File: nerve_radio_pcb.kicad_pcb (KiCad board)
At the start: 4 copper layers, 50 x 50 mm, 12 parts, among them J1 2x15, J2 5V UART Breakout, J3 3V SPI Breakout, J4 5V GPIO Breakout, U1 XBP9B-DMWT-002, U2 TXB0104QPWRQ1

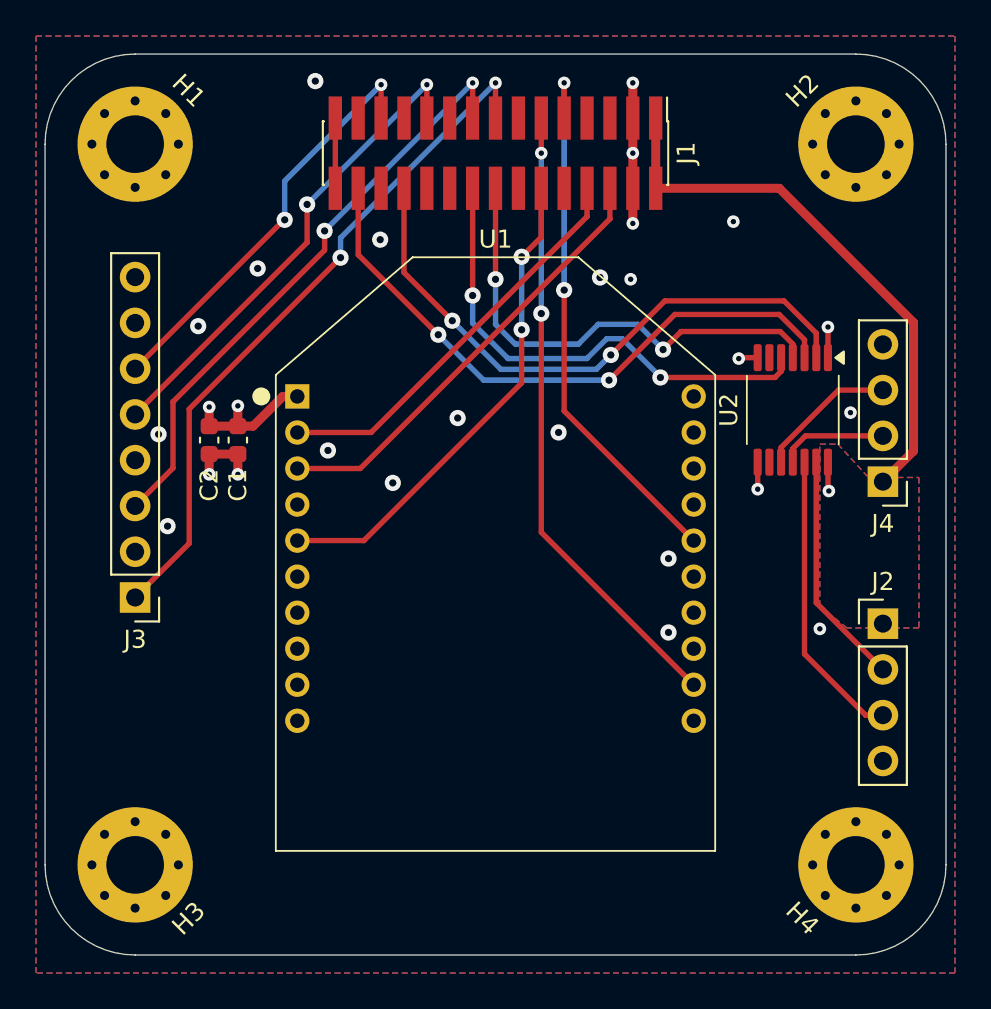
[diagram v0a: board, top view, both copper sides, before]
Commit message: Add ground stitching vias and silkscreen cleanup
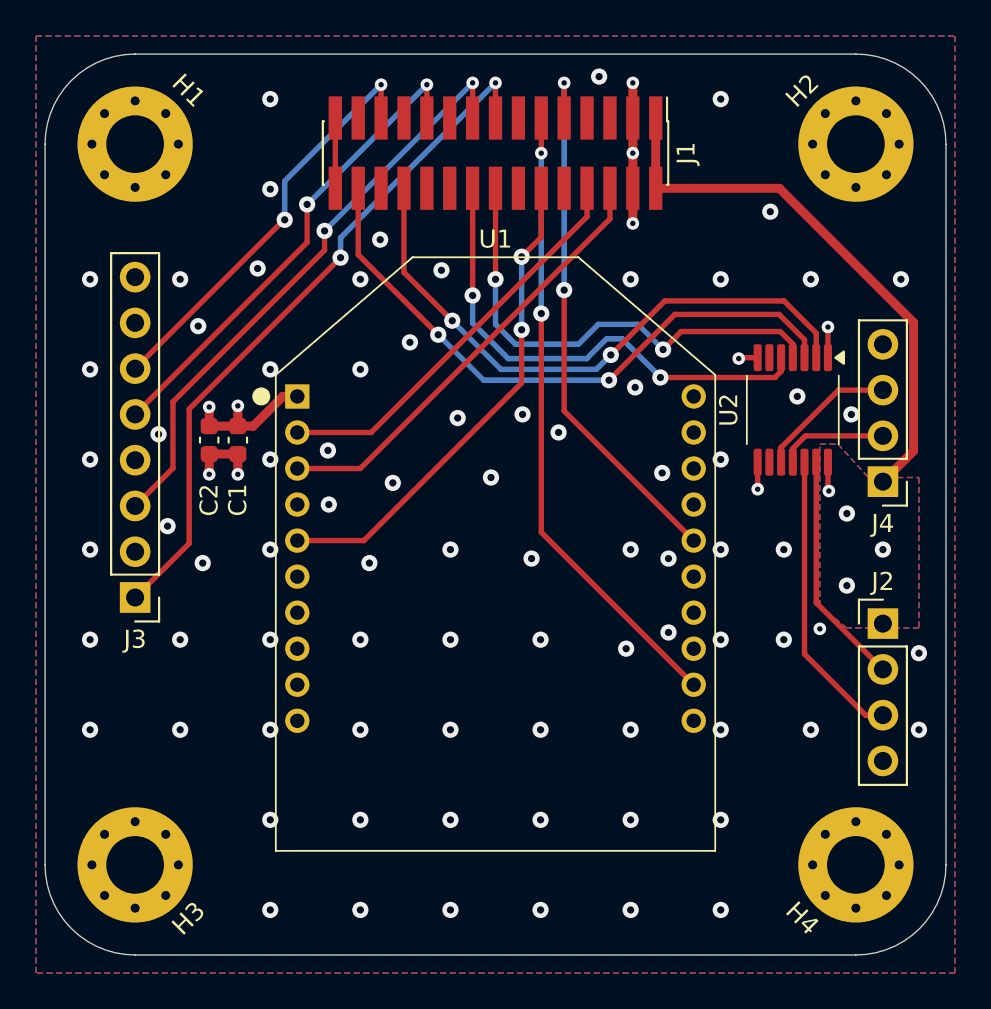
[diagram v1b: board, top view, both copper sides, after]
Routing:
- net GND: vias 20 -> 83
- net +5V: vias 1 -> 4

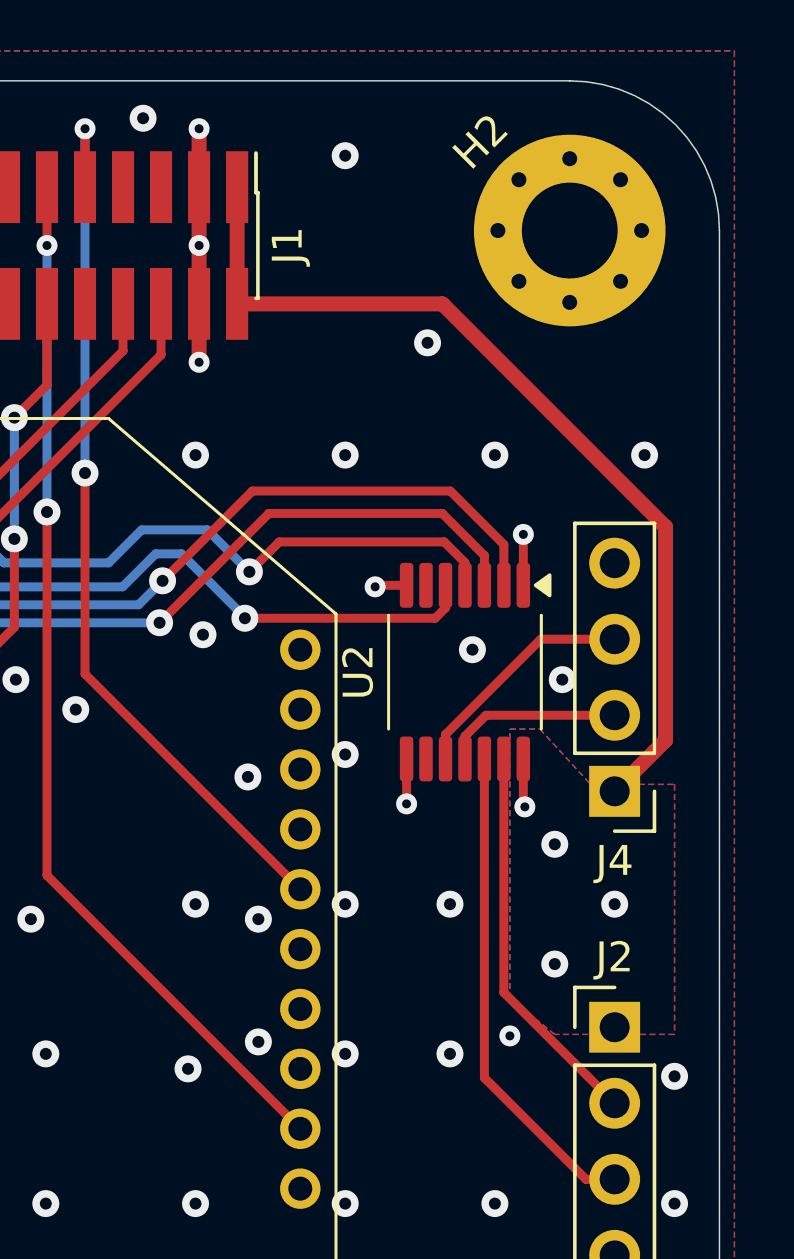
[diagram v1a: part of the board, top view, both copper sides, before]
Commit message: Widen 5V rail
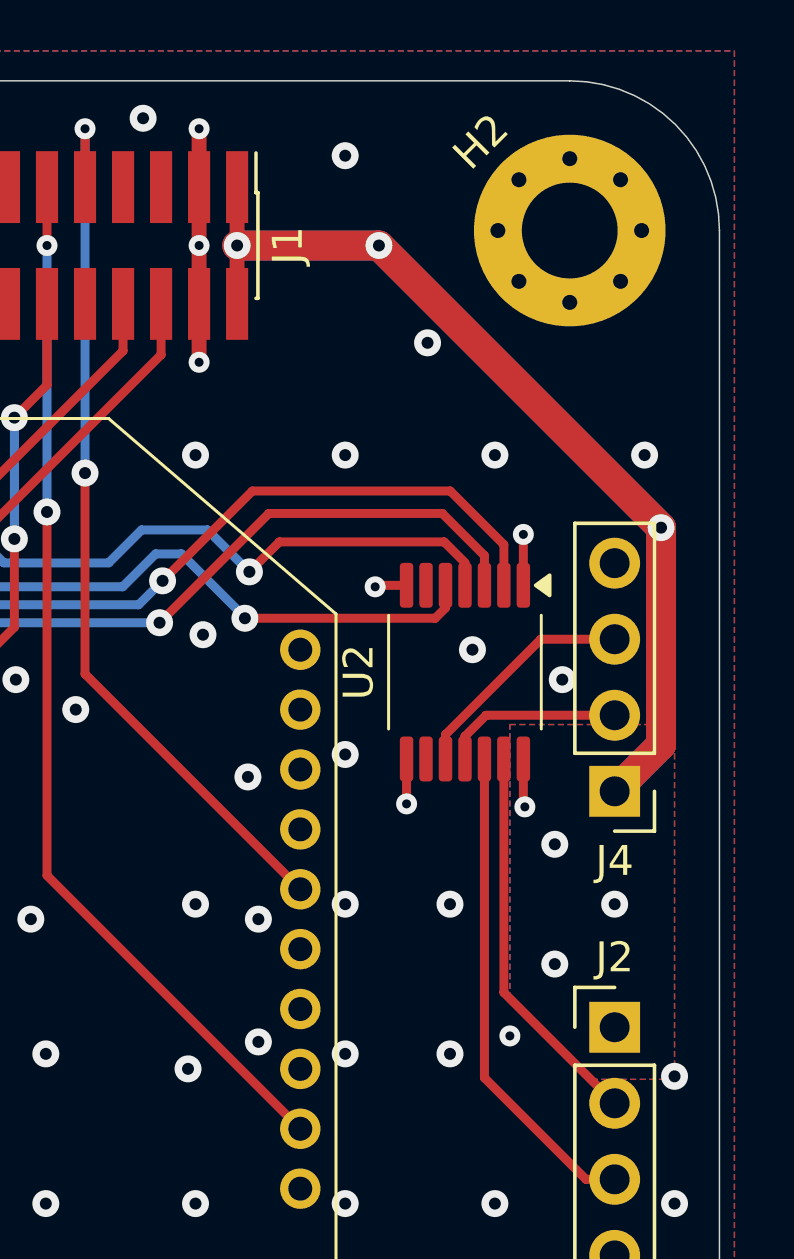
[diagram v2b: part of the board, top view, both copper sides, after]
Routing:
- net +5V: track 32.5 -> 60.5 mm, vias 4 -> 7
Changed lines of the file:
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@@
 	)
 	(segment
-		(start 157.39 83.55)
+		(start 171.55 102.18)
+		(end 171.55 94.923654)
+		(width 1)
+		(layer "F.Cu")
+		(net 4)
+	)
+	(segment
+		(start 157.39 85.5)
 		(end 157.39 87.45)
 		(width 0.5)
+		(layer "F.Cu")
+		(net 4)
+	)
+	(segment
+		(start 162.126346 85.5)
+		(end 157.39 85.5)
+		(width 1)
 		(layer "F.Cu")
 		(net 4)
@@
 	)
 	(segment
-		(start 171.7 94.9)
-		(end 171.7 102.03)
-		(width 0.5)
-		(layer "F.Cu")
-		(net 4)
-	)
-	(segment
 		(start 167 104.25)
 		(end 166.95 104.2)
@@
 	)
 	(segment
-		(start 164.25 87.45)
-		(end 171.7 94.9)
-		(width 0.5)
-		(layer "F.Cu")
-		(net 4)
-	)
-	(segment
-		(start 157.39 87.45)
-		(end 164.25 87.45)
-		(width 0.5)
-		(layer "F.Cu")
-		(net 4)
-	)
-	(segment
-		(start 171.7 102.03)
-		(end 170 103.73)
-		(width 0.5)
-		(layer "F.Cu")
+		(start 170 103.73)
+		(end 171.55 102.18)
+		(width 1)
+		(layer "F.Cu")
+		(net 4)
+	)
+	(segment
+		(start 171.55 94.923654)
+		(end 162.126346 85.5)
+		(width 1)
+		(layer "F.Cu")
+		(net 4)
+	)
+	(segment
+		(start 157.39 83.55)
+		(end 157.39 85.5)
+		(width 0.5)
+		(layer "F.Cu")
+		(net 4)
+	)
+	(via
+		(at 162.126346 85.5)
+		(size 0.9)
+		(drill 0.4)
+		(layers "F.Cu" "B.Cu")
 		(net 4)
 	)
@@
 	)
 	(via
+		(at 157.39 85.5)
+		(size 0.9)
+		(drill 0.4)
+		(layers "F.Cu" "B.Cu")
+		(net 4)
+	)
+	(via
 		(at 167 104.25)
 		(size 0.7)
@@
 		(layers "F.Cu" "B.Cu")
 		(free yes)
+		(net 4)
+	)
+	(via
+		(at 171.55 94.923654)
+		(size 0.9)
+		(drill 0.4)
+		(layers "F.Cu" "B.Cu")
+		(net 4)
+	)
+	(segment
+		(start 171.55 94.923654)
+		(end 162.126346 85.5)
+		(width 1)
+		(layer "B.Cu")
+		(net 4)
+	)
+	(segment
+		(start 171.55 102.18)
+		(end 171.55 94.923654)
+		(width 1)
+		(layer "B.Cu")
+		(net 4)
+	)
+	(segment
+		(start 170 103.73)
+		(end 171.55 102.18)
+		(width 1)
+		(layer "B.Cu")
+		(net 4)
+	)
+	(segment
+		(start 162.126346 85.5)
+		(end 157.39 85.5)
+		(width 1)
+		(layer "B.Cu")
 		(net 4)
 	)
@@
 		(polygon
 			(pts
-				(xy 172 111.85) (xy 168 111.85) (xy 166.5 110.65) (xy 166.5 101.65) (xy 167.5 101.65) (xy 169.2 103.5)
-				(xy 172 103.5)
+				(xy 172 113.35) (xy 169.25 113.35) (xy 166.5 110.65) (xy 166.5 101.5) (xy 172 101.5)
 			)
 		)

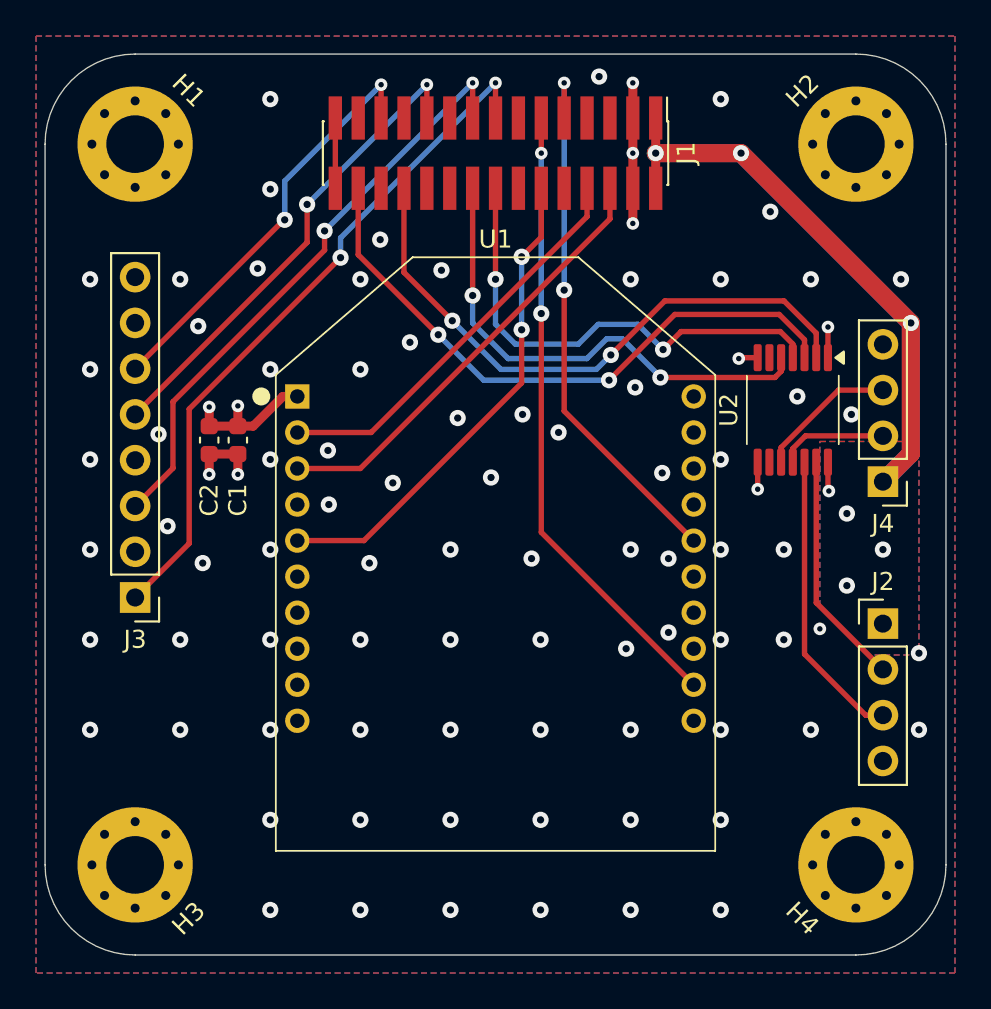
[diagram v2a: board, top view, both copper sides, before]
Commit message: Cleanup revision and docs pictures
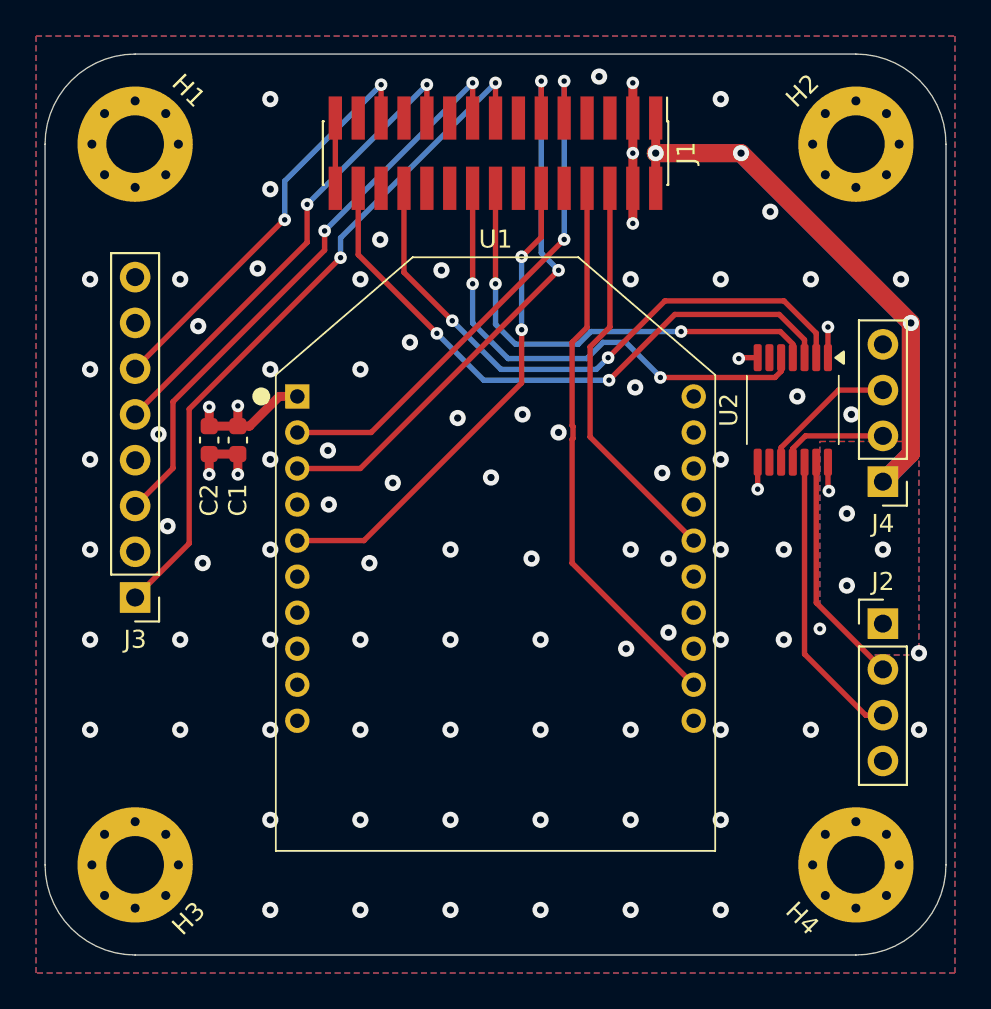
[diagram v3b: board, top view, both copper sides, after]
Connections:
- J1 pad 11: /RADIO_UART_CTS -> /RADIO_UART_TX
- J1 pad 6: /RADIO_UART_TX -> /RADIO_UART_RTS
- J1 pad 8: /RADIO_UART_RX -> /RADIO_UART_CTS
- J1 pad 9: /RADIO_UART_RTS -> /RADIO_UART_RX
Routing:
- net /RADIO_UART_RTS: track 30.3 -> 22.4 mm, vias 2 -> 0
- net /RADIO_UART_RX: track 22.6 -> 30.1 mm, vias 0 -> 2
- net /RADIO_UART_TX: track 24.8 -> 32.0 mm, vias 0 -> 2
- net /RADIO_UART_CTS: track 35.0 -> 30.7 mm, vias 2 -> 0
- net /GPIO_1: track 27.0 -> 25.8 mm

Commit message: Cleanup and update board-to-board connector
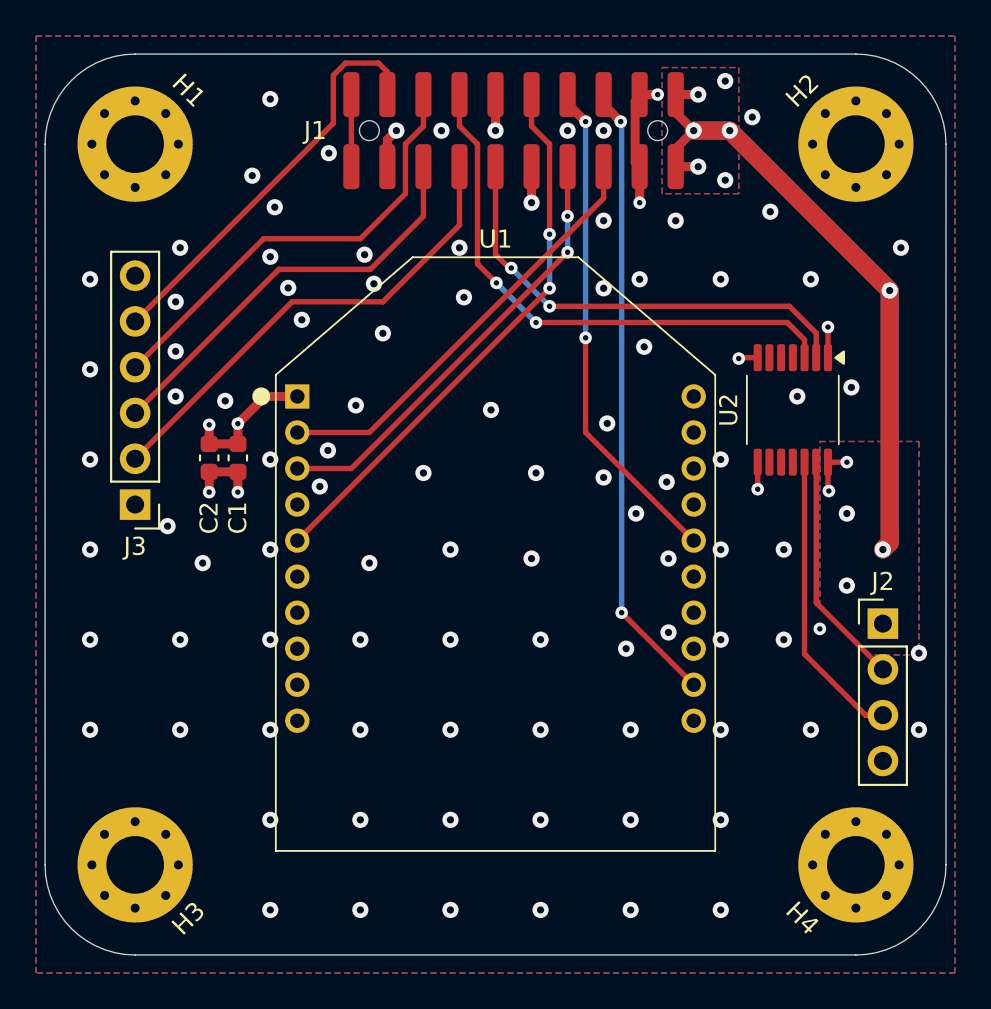
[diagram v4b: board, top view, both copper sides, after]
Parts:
- removed J4: 5V GPIO Breakout, Connector_PinHeader_2.54mm:PinHeader_1x04_P2.54mm_Vertical
- J1: value 2x15 -> BF030-20A-B1-0360-0277-0600-LB; footprint Connector_PinHeader_1.27mm:PinHeader_2x15_P1.27mm_Vertical_SMD -> connectors:bf030-20a-b1-0600-0277-0600-lb
- J2: value 5V UART Breakout -> 5V GPIO Breakout
- J3: footprint Connector_PinHeader_2.54mm:PinHeader_1x08_P2.54mm_Vertical -> Connector_PinHeader_2.54mm:PinHeader_1x06_P2.54mm_Vertical
- moved J3 5.16 mm to (128.5, 105.0)
- moved J1 1.60 mm to (149.5, 84.2), turned to 180 degrees
- moved C1 0.99 mm to (134.2, 102.4)
- moved C2 0.99 mm to (132.6, 102.4)
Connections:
- net /UART_RX_{5V} renamed /GPIO_1/PWM_1_{5V}
- net /UART_TX_{5V} renamed /GPIO_2/PWM_2_{5V}
- J1 pad 10: GND -> /RADIO_NRST
- J1 pad 11: /RADIO_UART_TX -> /GPIO_1/PWM_1
- J1 pad 12: /RADIO_NRST -> GND
- J1 pad 13: GND -> /SPI_MISO
- J1 pad 14: GND -> /GPIO_2/PWM_2
- J1 pad 15: /SPI_CS -> /SPI_MOSI
- J1 pad 16: /GPIO_1 -> /SPI_CLK
- J1 pad 17: /SPI_CLK -> GND
- J1 pad 18: /GPIO_2 -> /SPI_CS
- J1 pad 19: GND -> Net-(J1-Pad19)
- J1 pad 20: GND -> Net-(J1-Pad19)
- J1 pad 5: GND -> /RADIO_UART_RX
- J1 pad 6: /RADIO_UART_RTS -> /RADIO_UART_CTS
- J1 pad 7: GND -> /RADIO_UART_TX
- J1 pad 8: /RADIO_UART_CTS -> /RADIO_UART_RTS
- J1 pad 9: /RADIO_UART_RX -> GND
- J3 pad 1: /SPI_CS -> +3V3
- J3 pad 2: GND -> /SPI_MISO
- J3 pad 3: /SPI_CLK -> /SPI_MOSI
- J3 pad 4: GND -> /SPI_CLK
- J3 pad 5: /SPI_MISO -> /SPI_CS
- J3 pad 6: /SPI_MOSI -> GND
- U2 pad 10: /GPIO_2_{5V} -> unconnected-(U2-B4-Pad10)
- U2 pad 11: /GPIO_1_{5V} -> unconnected-(U2-B3-Pad11)
- U2 pad 2: /UART_RX -> /GPIO_1/PWM_1
- U2 pad 3: /UART_TX -> /GPIO_2/PWM_2
- U2 pad 4: /GPIO_1 -> unconnected-(U2-A3-Pad4)
- U2 pad 5: /GPIO_2 -> unconnected-(U2-A4-Pad5)
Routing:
- net /UART_TX: track 34.4 -> 0.00 mm, vias 2 -> 0
- net /UART_RX: track 33.5 -> 0.00 mm, vias 2 -> 0
- net /GPIO_2/PWM_2: track 0.00 -> 30.7 mm, vias 0 -> 2
- net /GPIO_2: track 27.5 -> 0.00 mm, vias 2 -> 0
- net /GPIO_1: track 25.8 -> 0.00 mm, vias 2 -> 0
- net /GPIO_1/PWM_1: track 0.00 -> 25.8 mm, vias 0 -> 2
- net /SPI_CS: track 38.8 -> 23.0 mm, vias 2 -> 0
- net /SPI_CLK: track 33.2 -> 24.9 mm, vias 2 -> 0
- net /GPIO_2_{5V}: track 7.78 -> 0.00 mm
- net +5V: track 60.5 -> 68.2 mm, vias 7 -> 12
- net /RADIO_UART_TX: track 32.0 -> 24.7 mm
- net GND: track 4.91 -> 11.1 mm, vias 83 -> 97
- net /GPIO_1_{5V}: track 6.05 -> 0.00 mm
- net /RADIO_UART_RX: track 30.1 -> 24.1 mm, vias 2 -> 0
- net /RADIO_UART_RTS: track 22.4 -> 27.7 mm, vias 0 -> 2
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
